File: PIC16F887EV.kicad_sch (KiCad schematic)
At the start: 91 parts, among them P1 USB_C_Plug_USB2.0, Q1 2N3904, Q2 2N3904, Q3 2N3904, Q5 2N3904, SW1 SW_Push, SW10 SW_Push, SW11 SW_Push, SW12 SW_Push, SW13 SW_Push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

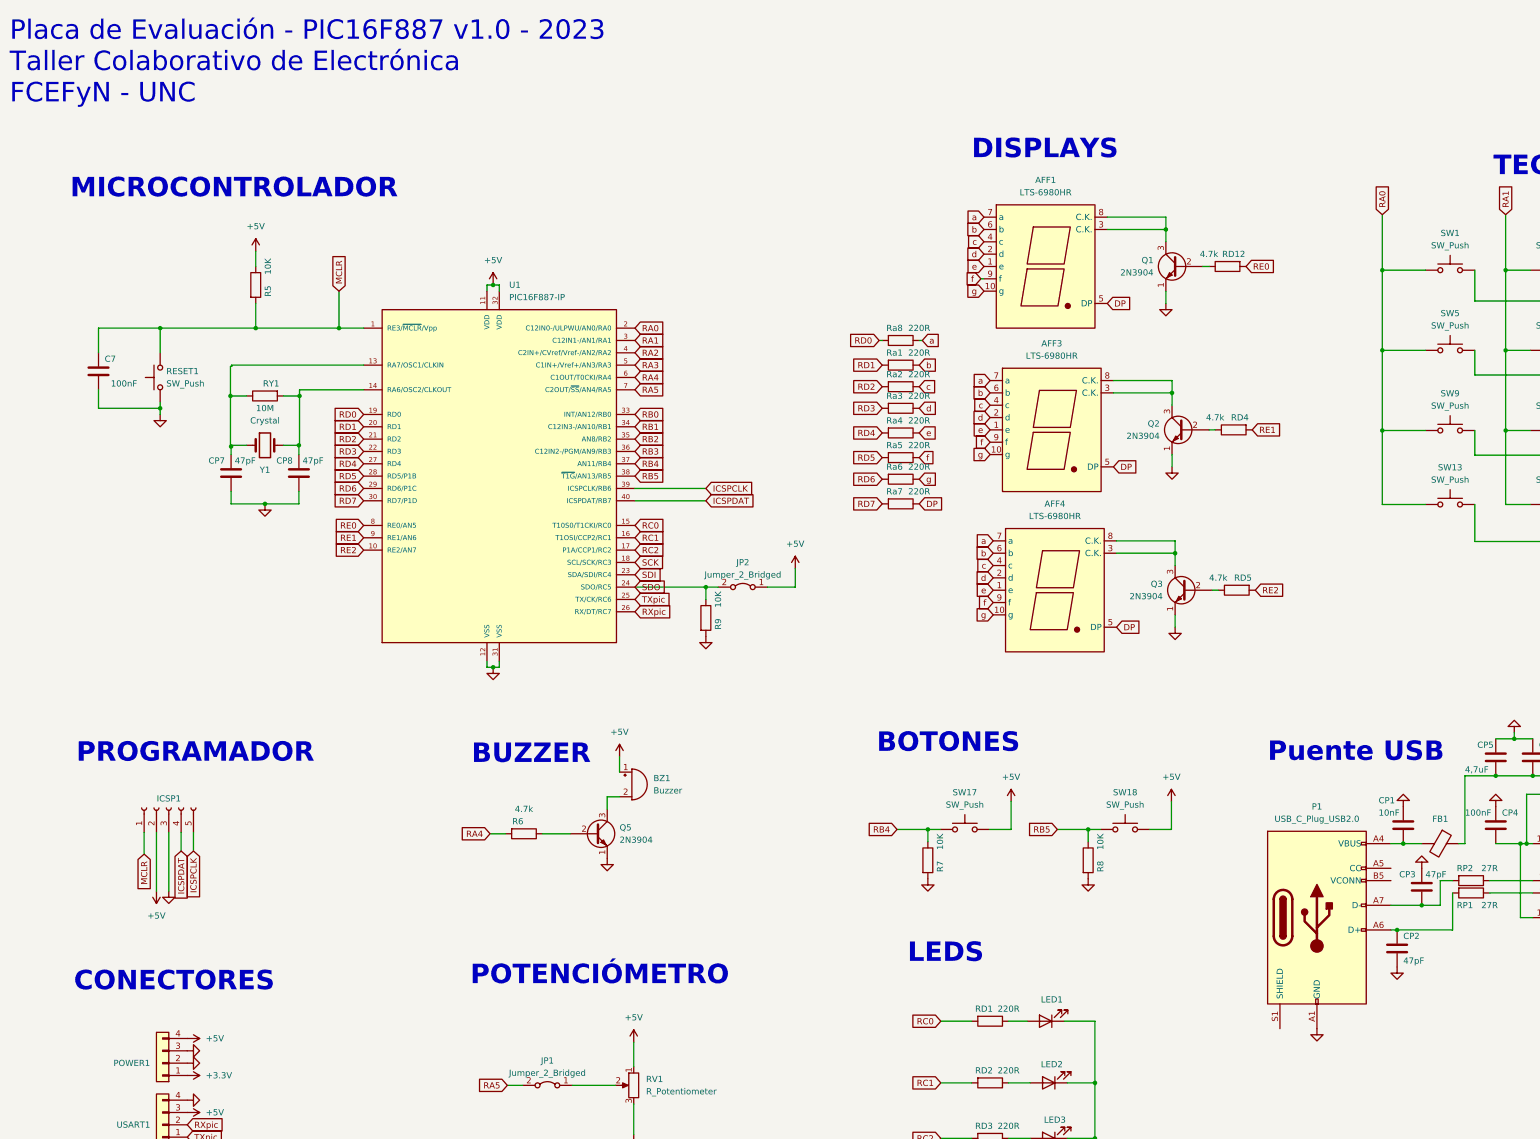
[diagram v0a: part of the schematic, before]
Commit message: Update v1.1
-Correccion USB C (pads, conexion shield, pines de datos, etc)
-Correccion footprints transistores, reruteo
-Se acomodaron los textos en silkscreen
-Zonas sin alivios termicos
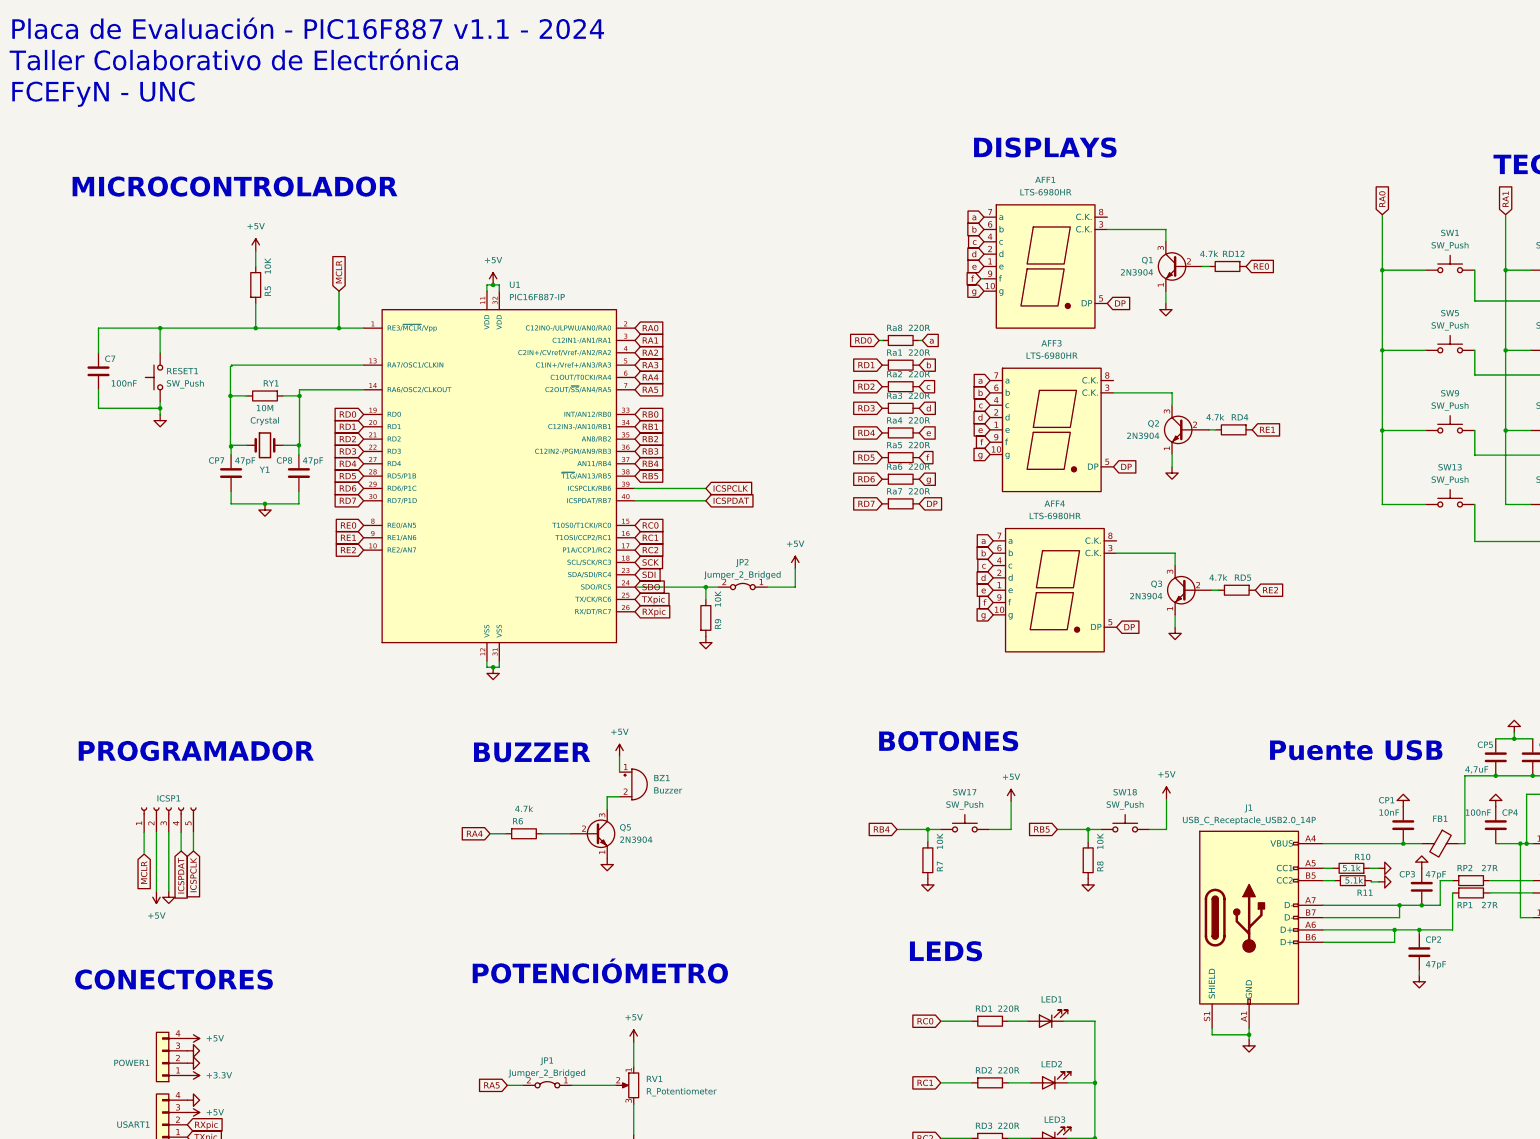
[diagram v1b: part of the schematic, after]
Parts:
- removed P1: USB_C_Plug_USB2.0, Connector_USB:USB_C_Receptacle_GCT_USB4105-xx-A_16P_TopMnt_Horizontal, symbol Connector:USB_C_Plug_USB2.0
- added J1: USB_C_Receptacle_USB2.0_14P, Connector_USB:USB_C_Receptacle_GCT_USB4105-xx-A_16P_TopMnt_Horizontal, symbol Connector:USB_C_Receptacle_USB2.0_14P
- added R10, R11: 5.1k, Resistor_SMD:R_1206_3216Metric_Pad1.30x1.75mm_HandSolder, symbol Device:R
- Q1, Q2, Q3, Q5, QP1, QP2: footprint Package_TO_SOT_SMD:SOT-23_Handsoldering -> Huellas:SOT-23_Handsoldering-mod
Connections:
- net GND: now also J1.A1 (GND), J1.A12 (GND), J1.B1 (GND), J1.B12 (GND), J1.S1 (SHIELD), R10.2, R11.2
- net at CP2.1, RP1.2: now also J1.A6 (D+), J1.B6 (D+)
- net at AFF4.3 (C.K.), Q3.3 (C): no longer AFF4.8 (C.K.)
- net at AFF3.3 (C.K.), Q2.3 (C): no longer AFF3.8 (C.K.)
- net at CP3.1, RP2.2: now also J1.A7 (D-), J1.B7 (D-)
- net at CP1.2, FB1.2: now also J1.A4 (VBUS), J1.A9 (VBUS), J1.B4 (VBUS), J1.B9 (VBUS)
- net at AFF1.3 (C.K.), Q1.3 (C): no longer AFF1.8 (C.K.)
- new net: J1.B5 (CC2), R11.1
- new net: J1.A5 (CC1), R10.1
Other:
- note added: "Placa de Evaluación - PIC16F887 v1.1 - 2024 Taller Colaborativo de Electrónica FCEFyN - UNC"
- note removed: "Placa de Evaluación - PIC16F887 v1.0 - 2023 Taller Colaborativo de Electrónica FCEFyN - UNC"
- moved on the sheet: CP2
